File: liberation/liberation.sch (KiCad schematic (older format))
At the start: 12 parts

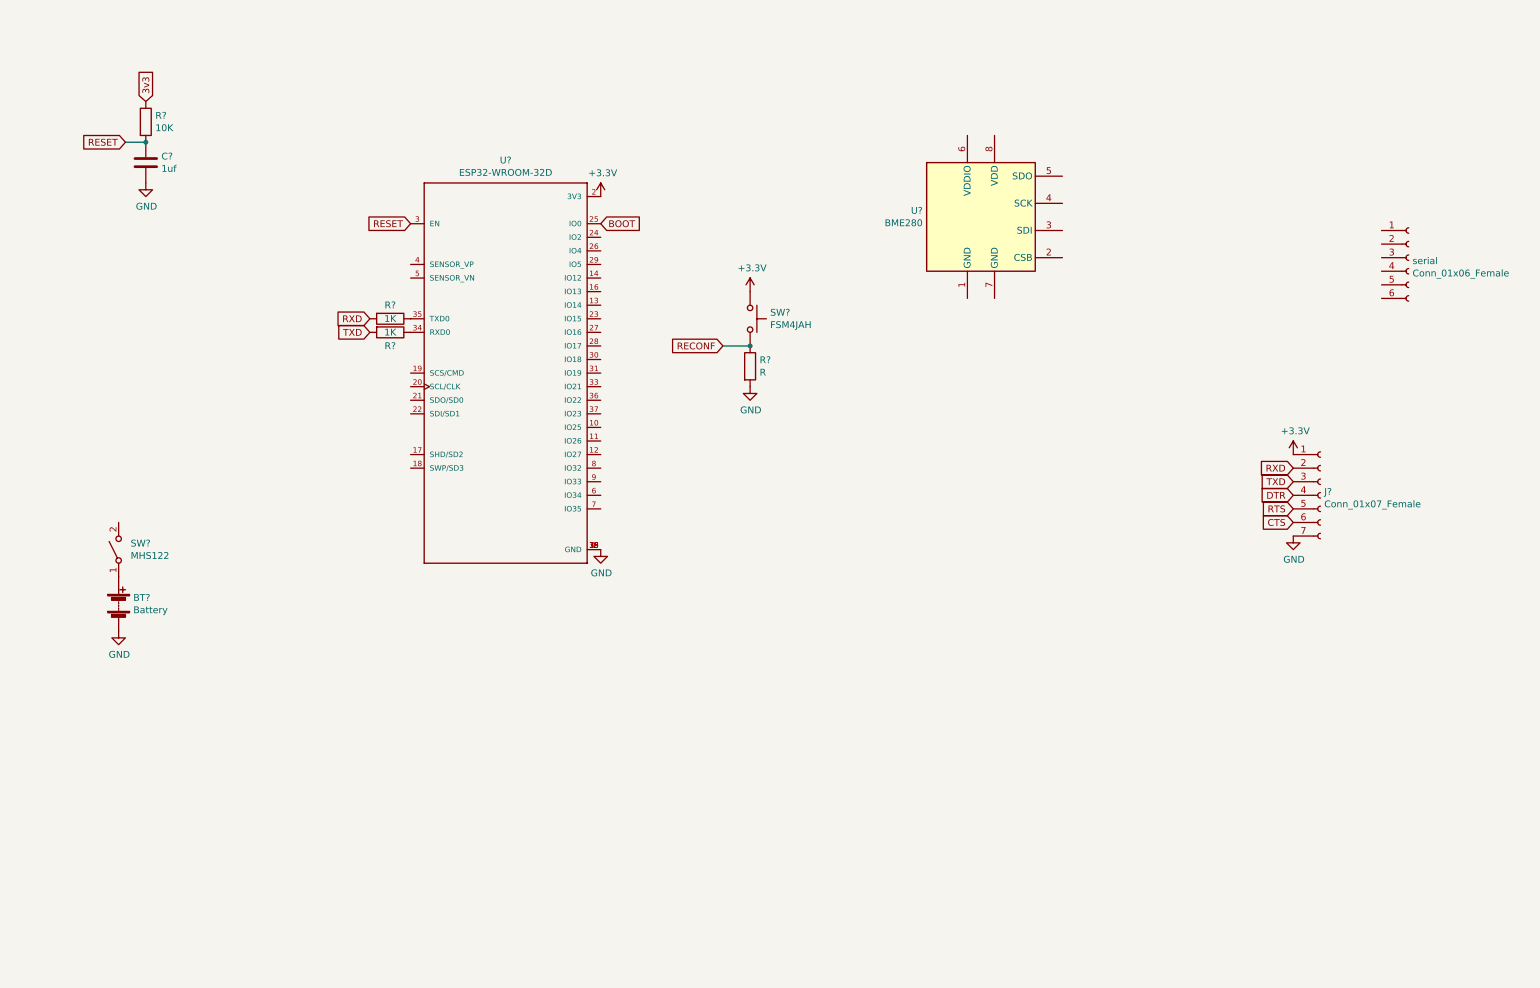
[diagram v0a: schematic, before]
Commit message: making i2c conection and boot reset
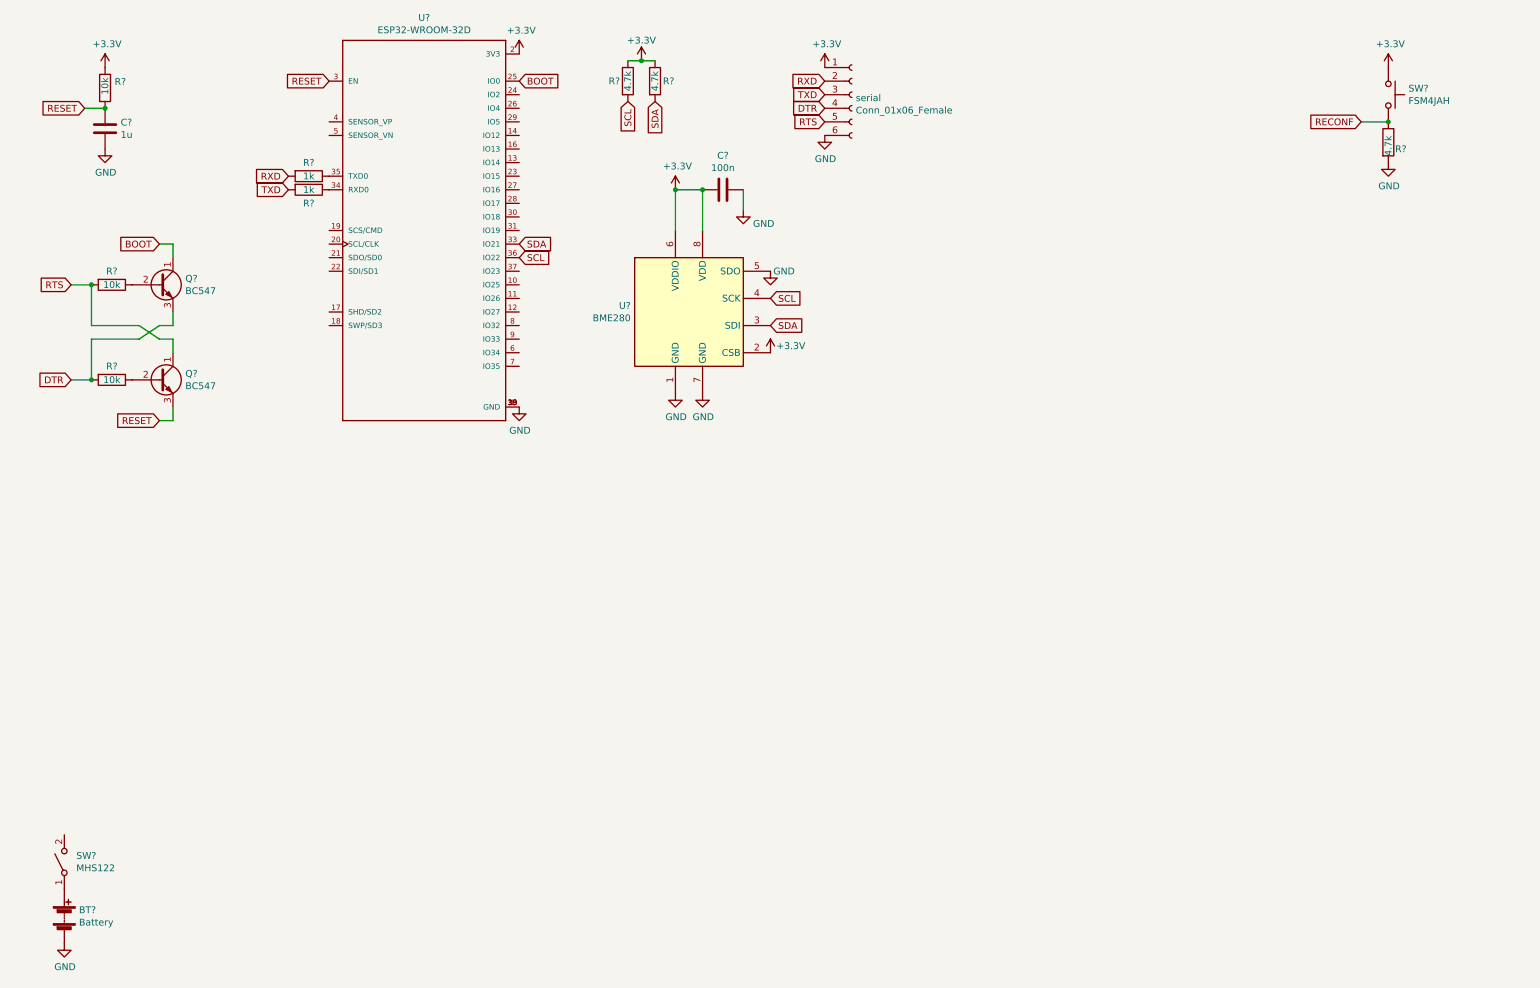
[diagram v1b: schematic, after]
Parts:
- removed J?: Conn_01x07_Female, symbol Connector:Conn_01x07_Female
- added C?: 100n, symbol Device:C
- added Q? (x2): BC547, Package_TO_SOT_THT:TO-92_Inline, symbol Transistor_BJT:BC547
- added R? (x2): 10k, symbol Device:R
- added R? (x2): 4.7k, symbol Device:R
- C?: value 1uf -> 1u
- R? (x2): value 1K -> 1k
- R?: value 10K -> 10k
- R?: value R -> 4.7k
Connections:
- net 3v3 is gone; now on net +3V3: R?.1
- net +3V3: now also U?.2 (CSB), U?.6 (VDDIO), U?.8 (VDD), serial.1 (Pin_1), C?.2, R?.1, R?.1
- net BOOT: now also Q?.1 (C)
- net DTR: now also serial.4 (Pin_4), Q?.3 (E), R?.2
- net GND: now also U?.1 (GND), U?.5 (SDO), U?.7 (GND), serial.6 (Pin_6), C?.1
- net RESET: now also Q?.3 (E)
- net RTS: now also serial.5 (Pin_5), Q?.1 (C), R?.2
- net RXD: now also serial.2 (Pin_2)
- net TXD: now also serial.3 (Pin_3)
- net SDA: now reaches U?.33 (IO21)
- net SDA: now also U?.3 (SDI), R?.2
- net SCL: now reaches U?.36 (IO22)
- net SCL: now also U?.4 (SCK), R?.2
- new net: Q?.2 (B), R?.1 (x2)
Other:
- moved on the sheet: BT?, C?, R?, SW?, U?, serial

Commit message: add liniar voltige regulator
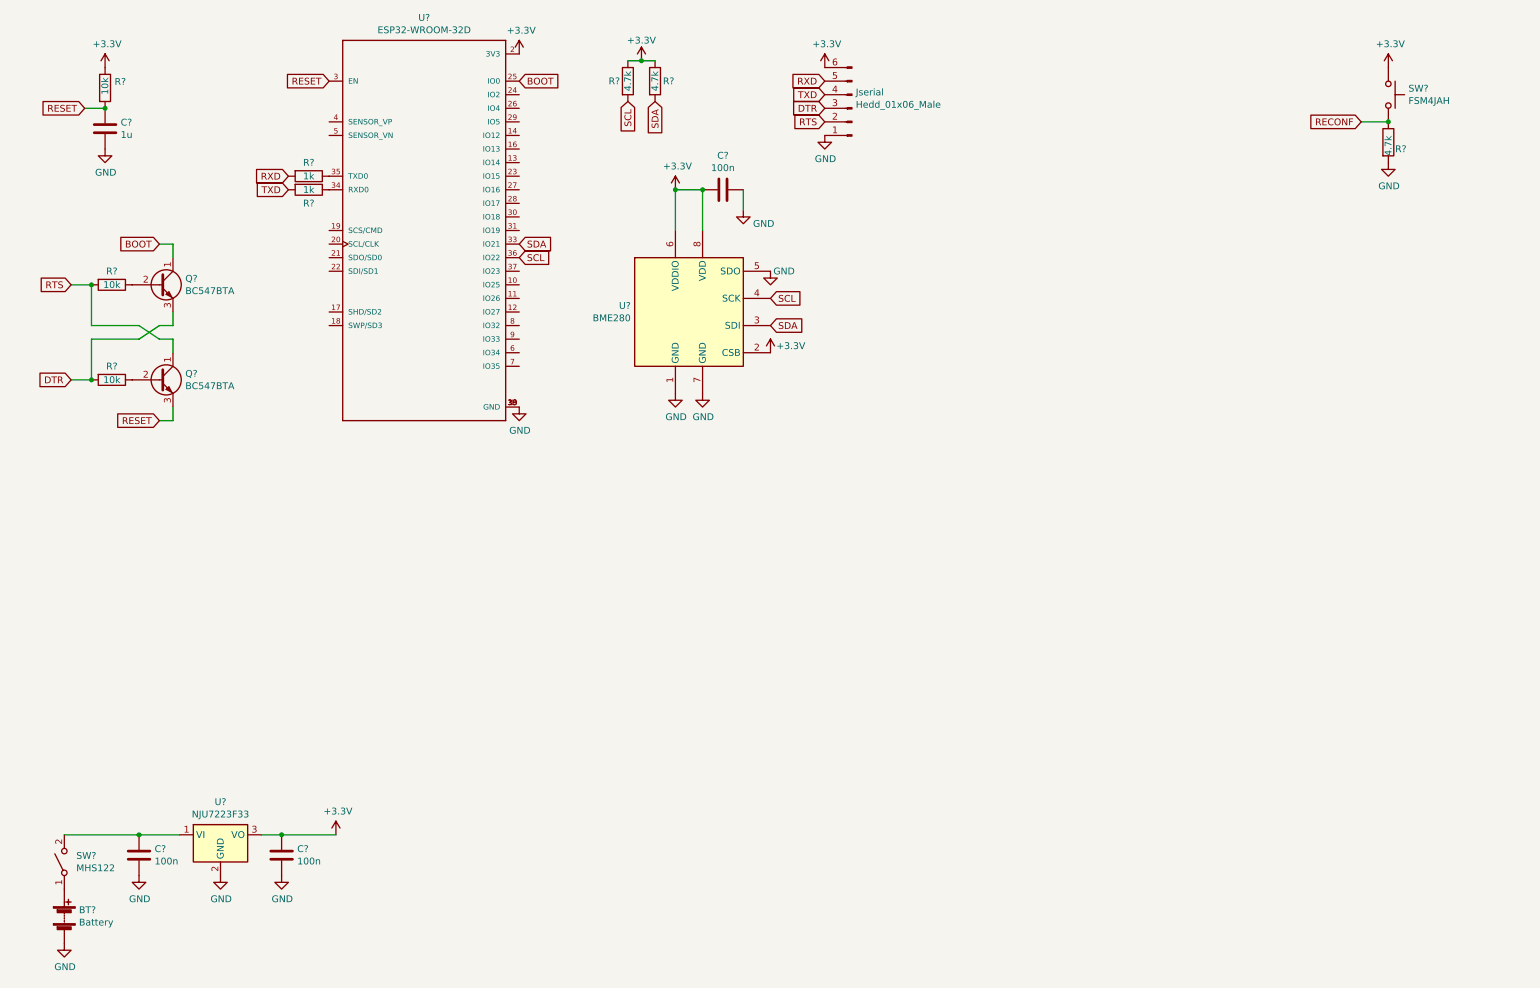
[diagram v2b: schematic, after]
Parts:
- removed serial: Conn_01x06_Female, symbol Connector:Conn_01x06_Female
- added C? (x2): 100n, symbol Device:C
- added Jserial: Hedd_01x06_Male, symbol Connector:Conn_01x06_Male
- added U?: NJU7223F33, symbol Regulator_Linear:MCP1825S
- Q? (x2): value BC547 -> BC547BTA
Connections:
- net +3V3: now also C?.1, Jserial.6 (Pin_6), U?.3 (VO)
- net DTR: now also Jserial.3 (Pin_3)
- net GND: now also C?.2, C?.2, Jserial.1 (Pin_1), U?.2 (GND)
- net RTS: now also Jserial.2 (Pin_2)
- net RXD: now also Jserial.5 (Pin_5)
- net TXD: now also Jserial.4 (Pin_4)
- net at SW?.2 (B): now also C?.1, U?.1 (VI)
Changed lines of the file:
@@
-	1    0    0    -1
-$EndComp
-$Comp
-L Connector:Conn_01x06_Female serial
-U 1 1 5DCF2976
-P 6700 1100
-F 0 "serial" H 6728 1076 50  0000 L CNN
-F 1 "Conn_01x06_Female" H 6728 985 50  0000 L CNN
-F 2 "" H 6700 1100 50  0001 C CNN
-F 3 "~" H 6700 1100 50  0001 C CNN
-	1    6700 1100
 	1    0    0    -1
 $EndComp
@@
 P 1600 3200
 F 0 "Q?" H 1791 3246 50  0000 L CNN
-F 1 "BC547" H 1791 3155 50  0000 L CNN
+F 1 "BC547BTA" H 1791 3155 50  0000 L CNN
 F 2 "Package_TO_SOT_THT:TO-92_Inline" H 1800 3125 50  0001 L CIN
 F 3 "http://www.fairchildsemi.com/ds/BC/BC547.pdf" H 1600 3200 50  0001 L CNN
@@
 P 1600 2500
 F 0 "Q?" H 1791 2546 50  0000 L CNN
-F 1 "BC547" H 1791 2455 50  0000 L CNN
+F 1 "BC547BTA" H 1791 2455 50  0000 L CNN
 F 2 "Package_TO_SOT_THT:TO-92_Inline" H 1800 2425 50  0001 L CIN
 F 3 "http://www.fairchildsemi.com/ds/BC/BC547.pdf" H 1600 2500 50  0001 L CNN
@@
 Text GLabel 6100 2800 2    50   Input ~ 0
 SDA
+$Comp
+L Regulator_Linear:MCP1825S U?
+U 1 1 5DD80B21
+P 2050 6550
+F 0 "U?" H 2050 6792 50  0000 C CNN
+F 1 "NJU7223F33" H 2050 6701 50  0000 C CNN
+F 2 "" H 1950 6700 50  0001 C CNN
+F 3 "http://ww1.microchip.com/downloads/en/devicedoc/22056b.pdf" H 2050 6800 50  0001 C CNN
+	1    2050 6550
+	1    0    0    -1
+$EndComp
+Wire Wire Line
+	900  6550 1450 6550
+$Comp
+L power:+3.3V #PWR?
+U 1 1 5DD823F0
+P 2900 6550
+F 0 "#PWR?" H 2900 6400 50  0001 C CNN
+F 1 "+3.3V" H 2915 6723 50  0000 C CNN
+F 2 "" H 2900 6550 50  0001 C CNN
+F 3 "" H 2900 6550 50  0001 C CNN
+	1    2900 6550
+	1    0    0    -1
+$EndComp
+$Comp
+L Device:C C?
+U 1 1 5DD82D83
+P 1450 6700
+F 0 "C?" H 1565 6746 50  0000 L CNN
+F 1 "100n" H 1565 6655 50  0000 L CNN
+F 2 "" H 1488 6550 50  0001 C CNN
+F 3 "~" H 1450 6700 50  0001 C CNN
+	1    1450 6700
+	1    0    0    -1
+$EndComp
+$Comp
+L Device:C C?
+U 1 1 5DD8579B
+P 2500 6700
+F 0 "C?" H 2615 6746 50  0000 L CNN
+F 1 "100n" H 2615 6655 50  0000 L CNN
+F 2 "" H 2538 6550 50  0001 C CNN
+F 3 "~" H 2500 6700 50  0001 C CNN
+	1    2500 6700
+	1    0    0    -1
+$EndComp
+$Comp
+L power:GND #PWR?
+U 1 1 5DD86141
+P 1450 6850
+F 0 "#PWR?" H 1450 6600 50  0001 C CNN
+F 1 "GND" H 1455 6677 50  0000 C CNN
+F 2 "" H 1450 6850 50  0001 C CNN
+F 3 "" H 1450 6850 50  0001 C CNN
+	1    1450 6850
+	1    0    0    -1
+$EndComp
+$Comp
+L power:GND #PWR?
+U 1 1 5DD864EB
+P 2050 6850
+F 0 "#PWR?" H 2050 6600 50  0001 C CNN
+F 1 "GND" H 2055 6677 50  0000 C CNN
+F 2 "" H 2050 6850 50  0001 C CNN
+F 3 "" H 2050 6850 50  0001 C CNN
+	1    2050 6850
+	1    0    0    -1
+$EndComp
+$Comp
+L power:GND #PWR?
+U 1 1 5DD868EA
+P 2500 6850
+F 0 "#PWR?" H 2500 6600 50  0001 C CNN
+F 1 "GND" H 2505 6677 50  0000 C CNN
+F 2 "" H 2500 6850 50  0001 C CNN
+F 3 "" H 2500 6850 50  0001 C CNN
+	1    2500 6850
+	1    0    0    -1
+$EndComp
+Wire Wire Line
+	1450 6550 1750 6550
+Connection ~ 1450 6550
+Wire Wire Line
+	2350 6550 2500 6550
+Wire Wire Line
+	2500 6550 2900 6550
+Connection ~ 2500 6550
+$Comp
+L Connector:Conn_01x06_Male Jserial
+U 1 1 5DD8A7C9
+P 6700 1200
+F 0 "Jserial" H 6672 1082 50  0000 R CNN
+F 1 "Hedd_01x06_Male" H 6672 1173 50  0000 R CNN
+F 2 "" H 6700 1200 50  0001 C CNN
+F 3 "~" H 6700 1200 50  0001 C CNN
+	1    6700 1200
+	-1   0    0    1
+$EndComp
 $EndSCHEMATC

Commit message: schema en netlist af
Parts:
- R1, R2, R3, R4, R5, R6, R7, R8: renamed from R?; footprint (none) -> Resistor_THT:R_Axial_DIN0204_L3.6mm_D1.6mm_P7.62mm_Horizontal
- SW1: renamed from SW?; value MHS122 -> MHS122K
- SW2: renamed from SW?; footprint (none) -> Button_Switch_THT:SW_PUSH_6mm_H5mm
- U2: renamed from U?; footprint MODULE_ESP32-WROOM-32D -> ESP32-WROOM-32D:MODULE_ESP32-WROOM-32D
- gave numbers to parts that had none: 9
- renumbered Jserial to Jserial1
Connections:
- net VBAT: now reaches C2.1, SW1.2 (B), U1.1 (VI)
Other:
- note added: "Batery and ON/OFF switch"
- note added: "Liniar voltige regulator"
- note added: "Micro controller\n"
- note added: "Power on reset circuit"
- note added: "Program circuit"
- note added: "Reconfigure button\n"
- note added: "Sensor\n"
- note added: "Serial conector\n"
- note added: "i2c pullup resistors"
- moved on the sheet: BT1, C1, C2, C3, C4, Jserial1, Q1, Q2, R1, R2, R3, R4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

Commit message: scheam af nu
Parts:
- BT1: footprint (none) -> Battery:keystone_2477
- C1: footprint (none) -> Capacitor_THT:CP_Radial_D5.0mm_P2.00mm
- C2, C3, C4: footprint (none) -> Capacitor_THT:C_Disc_D4.7mm_W2.5mm_P5.00mm
- Jserial1: footprint (none) -> Connector_PinHeader_2.54mm:PinHeader_1x06_P2.54mm_Vertical
- SW1: footprint (none) -> Button_Switch_THT:MHS122
- U1: footprint (none) -> Package_TO_SOT_THT:TO-3P-3_Vertical
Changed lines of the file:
@@
 F 0 "C1" H 1915 1796 50  0000 L CNN
 F 1 "1u" H 1915 1705 50  0000 L CNN
-F 2 "" H 1838 1600 50  0001 C CNN
+F 2 "Capacitor_THT:CP_Radial_D5.0mm_P2.00mm" H 1838 1600 50  0001 C CNN
 F 3 "~" H 1800 1750 50  0001 C CNN
 	1    1800 1750
@@
 F 0 "BT1" H 1808 6846 50  0000 L CNN
 F 1 "Battery" H 1808 6755 50  0000 L CNN
-F 2 "" V 1700 6860 50  0001 C CNN
+F 2 "Battery:keystone_2477" V 1700 6860 50  0001 C CNN
 F 3 "~" V 1700 6860 50  0001 C CNN
 	1    1700 6800
@@
 F 0 "SW1" V 1746 6312 50  0000 R CNN
 F 1 "MHS122K" V 1655 6312 50  0000 R CNN
-F 2 "" H 1700 6400 50  0001 C CNN
+F 2 "Button_Switch_THT:MHS122" H 1700 6400 50  0001 C CNN
 F 3 "~" H 1700 6400 50  0001 C CNN
 	1    1700 6400
@@
 F 0 "C4" V 5648 3600 50  0000 C CNN
 F 1 "100n" V 5739 3600 50  0000 C CNN
-F 2 "" H 5938 3450 50  0001 C CNN
+F 2 "Capacitor_THT:C_Disc_D4.7mm_W2.5mm_P5.00mm" H 5938 3450 50  0001 C CNN
 F 3 "~" H 5900 3600 50  0001 C CNN
 	1    5900 3600
@@
 F 0 "U1" H 5000 6842 50  0000 C CNN
 F 1 "NJU7223F33" H 5000 6751 50  0000 C CNN
-F 2 "" H 4900 6750 50  0001 C CNN
+F 2 "Package_TO_SOT_THT:TO-3P-3_Vertical" H 4900 6750 50  0001 C CNN
 F 3 "http://ww1.microchip.com/downloads/en/devicedoc/22056b.pdf" H 5000 6850 50  0001 C CNN
 	1    5000 6600
@@
 F 0 "C2" H 4515 6796 50  0000 L CNN
 F 1 "100n" H 4515 6705 50  0000 L CNN
-F 2 "" H 4438 6600 50  0001 C CNN
+F 2 "Capacitor_THT:C_Disc_D4.7mm_W2.5mm_P5.00mm" H 4438 6600 50  0001 C CNN
 F 3 "~" H 4400 6750 50  0001 C CNN
 	1    4400 6750
@@
 F 0 "C3" H 5565 6796 50  0000 L CNN
 F 1 "100n" H 5565 6705 50  0000 L CNN
-F 2 "" H 5488 6600 50  0001 C CNN
+F 2 "Capacitor_THT:C_Disc_D4.7mm_W2.5mm_P5.00mm" H 5488 6600 50  0001 C CNN
 F 3 "~" H 5450 6750 50  0001 C CNN
 	1    5450 6750
@@
 F 0 "Jserial1" H 9422 1482 50  0000 R CNN
 F 1 "Hedd_01x06_Male" H 9422 1573 50  0000 R CNN
-F 2 "" H 9450 1600 50  0001 C CNN
+F 2 "Connector_PinHeader_2.54mm:PinHeader_1x06_P2.54mm_Vertical" H 9450 1600 50  0001 C CNN
 F 3 "~" H 9450 1600 50  0001 C CNN
 	1    9450 1600

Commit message: pcs begin
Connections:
- net RECONF: now also U2.16 (IO13)
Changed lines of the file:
@@
 Text Notes 4200 5750 2    50   ~ 0
 Liniar voltige regulator
+Text GLabel 9800 4000 2    50   Input ~ 0
+RECONF
 $EndSCHEMATC

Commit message: Make PCB design (almost) complete :p
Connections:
- net DTR: now also Jserial1.2 (Pin_2); no longer Jserial1.3 (Pin_3)
- net RTS: now also Jserial1.3 (Pin_3); no longer Jserial1.2 (Pin_2)
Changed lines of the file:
@@
 Text GLabel 9250 1500 0    50   Input ~ 0
 TXD
+Text GLabel 9250 1700 0    50   Input ~ 0
+DTR
 Text GLabel 9250 1600 0    50   Input ~ 0
-DTR
-Text GLabel 9250 1700 0    50   Input ~ 0
 RTS
 $Comp

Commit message: finich pcb and secmatic for ordering
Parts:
- U1: footprint Package_TO_SOT_THT:TO-3P-3_Vertical -> Package_TO_SOT_THT:NJU7223F33
- renumbered Q2 to Q1, Q1 to Q2, R3 to R2, R2 to R3, R5 to R4, R4 to R5
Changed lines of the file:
@@
 TXD
 $Comp
-L Device:R R5
+L Device:R R4
 U 1 1 5DCF7C7E
 P 8250 4300
-F 0 "R5" V 8350 4300 50  0000 C CNN
+F 0 "R4" V 8350 4300 50  0000 C CNN
 F 1 "1k" V 8250 4300 50  0000 C CNN
 F 2 "Resistor_THT:R_Axial_DIN0204_L3.6mm_D1.6mm_P7.62mm_Horizontal" V 8180 4300 50  0001 C CNN
@@
 $EndComp
 $Comp
-L Device:R R4
+L Device:R R5
 U 1 1 5DCF7556
 P 8250 4200
-F 0 "R4" V 8150 4200 50  0000 C CNN
+F 0 "R5" V 8150 4200 50  0000 C CNN
 F 1 "1k" V 8250 4200 50  0000 C CNN
 F 2 "Resistor_THT:R_Axial_DIN0204_L3.6mm_D1.6mm_P7.62mm_Horizontal" V 8180 4200 50  0001 C CNN
@@
 $EndComp
 $Comp
-L Device:R R2
+L Device:R R3
 U 1 1 5DCF56CC
 P 2050 3900
-F 0 "R2" V 1950 3900 50  0000 C CNN
+F 0 "R3" V 1950 3900 50  0000 C CNN
 F 1 "10k" V 2050 3900 50  0000 C CNN
 F 2 "Resistor_THT:R_Axial_DIN0204_L3.6mm_D1.6mm_P7.62mm_Horizontal" V 1980 3900 50  0001 C CNN
@@
 $EndComp
 $Comp
-L Device:R R3
+L Device:R R2
 U 1 1 5DCF64FD
 P 2050 4600
-F 0 "R3" V 1950 4600 50  0000 C CNN
+F 0 "R2" V 1950 4600 50  0000 C CNN
 F 1 "10k" V 2050 4600 50  0000 C CNN
 F 2 "Resistor_THT:R_Axial_DIN0204_L3.6mm_D1.6mm_P7.62mm_Horizontal" V 1980 4600 50  0001 C CNN
@@
 	2500 3600 2500 3700
 $Comp
-L Transistor_BJT:BC547 Q2
+L Transistor_BJT:BC547 Q1
 U 1 1 5DCF46FB
 P 2400 4600
-F 0 "Q2" H 2591 4646 50  0000 L CNN
+F 0 "Q1" H 2591 4646 50  0000 L CNN
 F 1 "BC547BTA" H 2591 4555 50  0000 L CNN
 F 2 "Package_TO_SOT_THT:TO-92_Inline" H 2600 4525 50  0001 L CIN
@@
 $EndComp
 $Comp
-L Transistor_BJT:BC547 Q1
+L Transistor_BJT:BC547 Q2
 U 1 1 5DCF3487
 P 2400 3900
-F 0 "Q1" H 2591 3946 50  0000 L CNN
+F 0 "Q2" H 2591 3946 50  0000 L CNN
 F 1 "BC547BTA" H 2591 3855 50  0000 L CNN
 F 2 "Package_TO_SOT_THT:TO-92_Inline" H 2600 3825 50  0001 L CIN
@@
 F 0 "U1" H 5000 6842 50  0000 C CNN
 F 1 "NJU7223F33" H 5000 6751 50  0000 C CNN
-F 2 "Package_TO_SOT_THT:TO-3P-3_Vertical" H 4900 6750 50  0001 C CNN
+F 2 "Package_TO_SOT_THT:NJU7223F33" H 4900 6750 50  0001 C CNN
 F 3 "http://ww1.microchip.com/downloads/en/devicedoc/22056b.pdf" H 5000 6850 50  0001 C CNN
 	1    5000 6600
